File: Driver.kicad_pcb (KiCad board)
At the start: 2 copper layers, 25.5 x 48 mm, 18 parts, among them J1 Screw_Terminal_01x05, U1 IS31FL3239, U2 AP2204K-ADJ

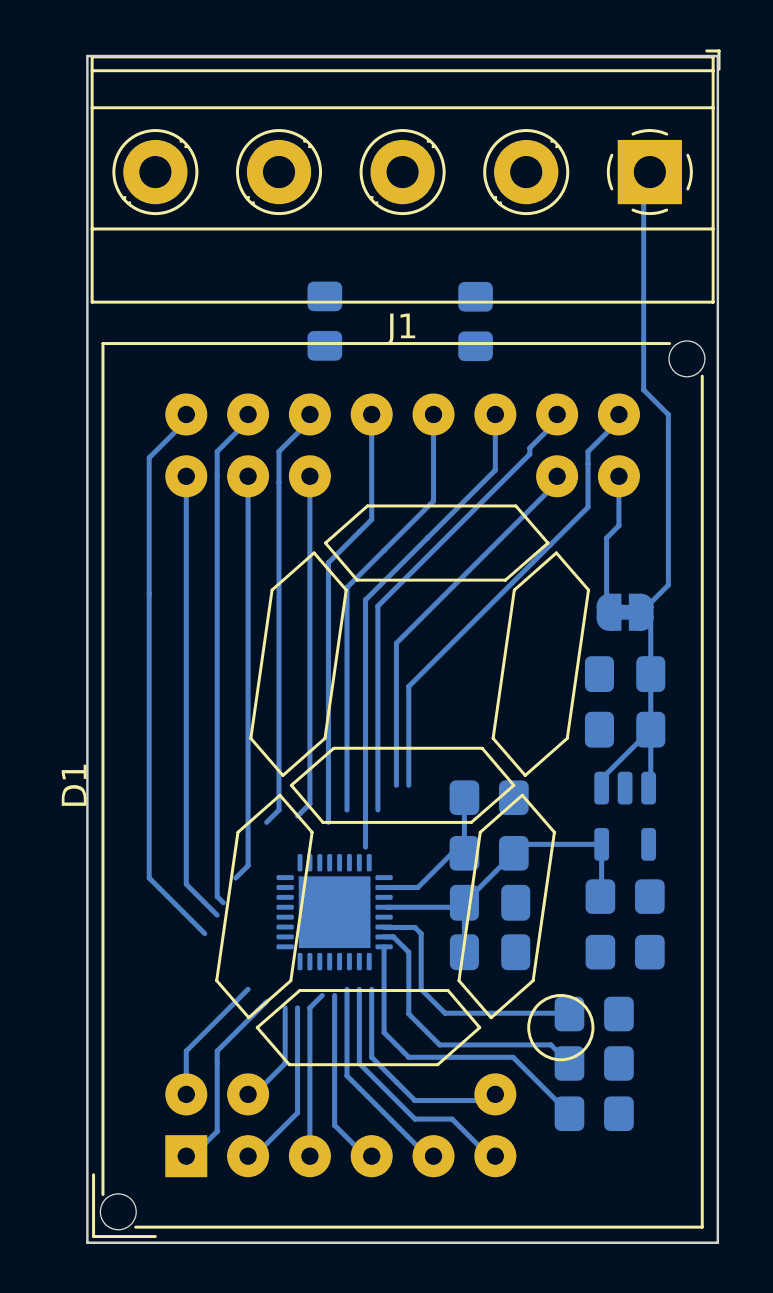
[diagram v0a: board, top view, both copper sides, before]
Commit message: PCB shows no errors, needs improvements before prototype
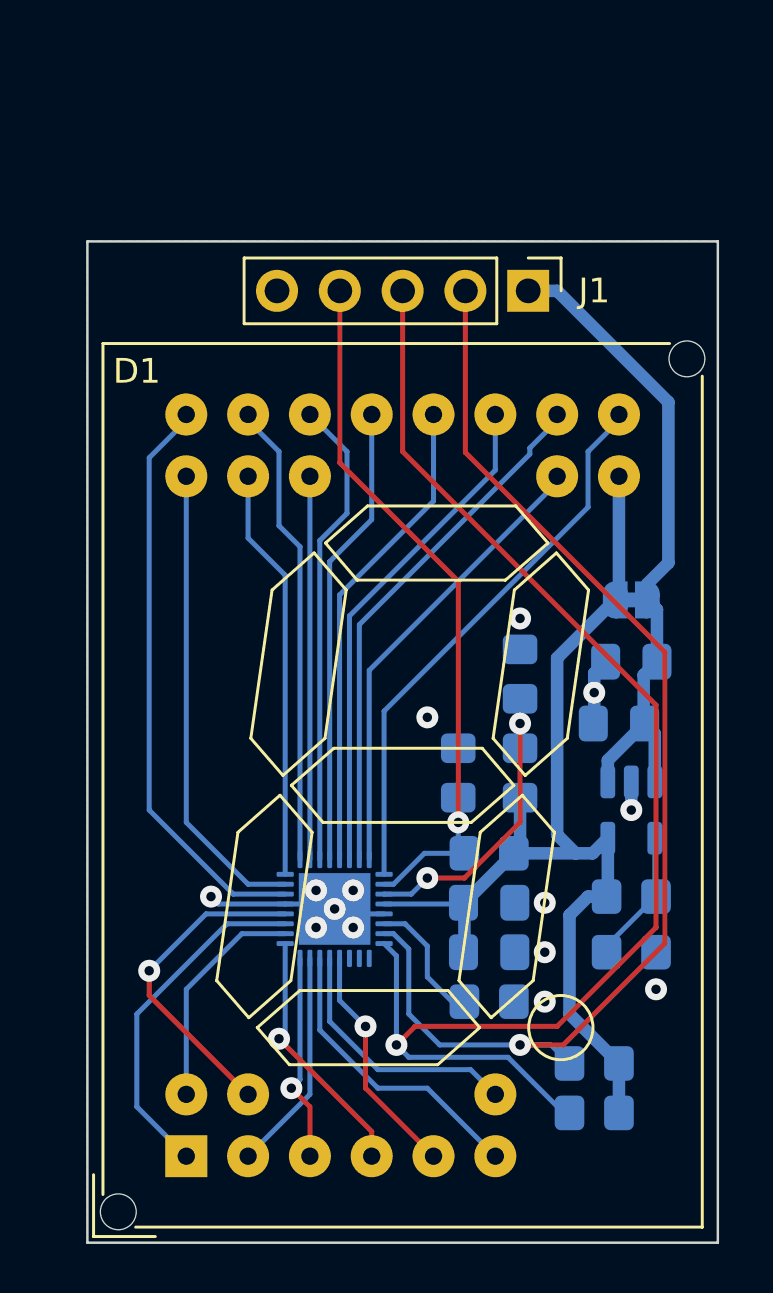
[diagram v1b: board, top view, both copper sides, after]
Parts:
- J1: value Screw_Terminal_01x05 -> Conn_01x05_Socket; footprint TerminalBlock_Phoenix:TerminalBlock_Phoenix_MKDS-1,5-5_1x05_P5.00mm_Horizontal -> Connector_PinHeader_2.54mm:PinHeader_1x05_P2.54mm_Vertical
- moved R4 18.3 mm to (205.0, 99.0)
- moved R10 16.3 mm to (205.0, 95.0)
- moved J1 6.88 mm to (205.3, 79.5), turned to -90 degrees
- moved R11 4.28 mm to (203.8, 108.2)
- moved R3 1.60 mm to (202.5, 99.0), turned to 90 degrees
- moved C2 0.56 mm to (209.5, 94.5)
- moved JP1 0.56 mm to (209.5, 92.0)
- moved C1 0.35 mm to (209.0, 97.0)
- moved U2 0.35 mm to (209.5, 100.5)
- moved R5 0.25 mm to (209.5, 104.0)
- moved R7 0.25 mm to (209.5, 106.2)
- moved U1 0.13 mm to (197.5, 104.5)
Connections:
- U1 pad 1: /LED_R1 -> unconnected-(U1-OUT1-Pad1)
- U1 pad 10: /LED_R4 -> /LED_B5
- U1 pad 11: /LED_G4 -> /LED_G5
- U1 pad 12: /LED_B4 -> /LED_R5
- U1 pad 14: /LED_R5 -> /LED_B6
- U1 pad 15: /LED_G5 -> /LED_G6
- U1 pad 16: /LED_B5 -> /LED_R6
- U1 pad 17: /LED_R6 -> /LED_B7
- U1 pad 18: /LED_G6 -> /LED_G7
- U1 pad 19: /LED_B6 -> /LED_R7
- U1 pad 2: /LED_G1 -> unconnected-(U1-OUT2-Pad2)
- U1 pad 20: /LED_R7 -> /LED_B1
- U1 pad 21: /LED_G7 -> /LED_G1
- U1 pad 22: /LED_B7 -> /LED_R1
- U1 pad 23: unconnected-(U1-OUT22-Pad23) -> /LED_B2
- U1 pad 24: unconnected-(U1-OUT23-Pad24) -> /LED_G2
- U1 pad 25: unconnected-(U1-OUT24-Pad25) -> /LED_R2
- U1 pad 3: /LED_B1 -> unconnected-(U1-OUT3-Pad3)
- U1 pad 4: /LED_R2 -> /LED_B3
- U1 pad 5: /LED_G2 -> /LED_G3
- U1 pad 6: /LED_B2 -> /LED_R3
- U1 pad 7: /LED_R3 -> /LED_B4
- U1 pad 8: /LED_G3 -> /LED_G4
- U1 pad 9: /LED_B3 -> /LED_R4
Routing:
- net /SCL: track 12.3 -> 54.9 mm, vias 0 -> 1
- net /SDA: track 11.1 -> 48.5 mm, vias 0 -> 1
- net VCC: track 19.4 -> 44.0 mm
- net /~{SDB}: track 5.99 -> 29.6 mm, vias 0 -> 1
- net /AD: track 0.00 -> 12.7 mm, vias 0 -> 2
- net GND: track 0.00 -> 11.7 mm, vias 0 -> 14
- net /LED_R5: track 4.37 -> 13.1 mm, vias 0 -> 1
- net /LED_G5: track 7.85 -> 14.1 mm
- net Net-(U2-ADJ): track 0.00 -> 5.46 mm
- net Net-(U1-ISET): track 10.3 -> 5.29 mm
- net /LED_R2: track 18.3 -> 22.3 mm
- net /LED_B5: track 5.54 -> 9.18 mm
- net /LED_G2: track 14.9 -> 18.4 mm
- net /LED_R4: track 7.37 -> 10.3 mm, vias 0 -> 1
- net /V_{in}: track 29.2 -> 26.8 mm
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- added copper zone on B.Cu, net GND
- added copper zone on F.Cu, net GND
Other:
- board size 25.5 x 48 mm -> 25.5 x 40.5 mm

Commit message: More updates/work. Close to finished board
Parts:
- removed C1: 1u, Capacitor_SMD:C_0805_2012Metric_Pad1.18x1.45mm_HandSolder
- removed C2: 0.1u, Capacitor_SMD:C_0805_2012Metric_Pad1.18x1.45mm_HandSolder
- removed JP1: Jumper_2_Bridged, Jumper:SolderJumper-2_P1.3mm_Bridged_RoundedPad1.0x1.5mm
- removed R7: 3.3k, Resistor_SMD:R_0805_2012Metric_Pad1.20x1.40mm_HandSolder
- removed U2: AP2204K-ADJ, Package_TO_SOT_SMD:SOT-23-5
- added J2: Conn_01x05_Socket, ProjectLibrary:CustomBoardInterconnectMirror, B.Cu at (191.5, 106.2)
- added J3: Conn_01x05_Pin, ProjectLibrary:CustomBoardInterconnect, B.Cu at (213.0, 106.2)
- added R6: 0, Resistor_SMD:R_0805_2012Metric_Pad1.20x1.40mm_HandSolder, B.Cu at (207.0, 98.5)
- R5: value 3.3k -> 0
- moved R5 9.82 mm to (207.0, 94.5), turned to -90 degrees
- moved R4 4.53 mm to (204.5, 94.5), turned to -90 degrees
- moved R10 3.54 mm to (204.5, 98.5), turned to 90 degrees
- moved R1 1.46 mm to (208.8, 114.0)
- moved R2 1.25 mm to (208.8, 111.8)
- moved R3 0.50 mm to (202.0, 99.0)
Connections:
- J1 pad 1: /V_{in} -> VCC
- J1 pad 4: /~{SDB} -> GND
- J1 pad 5: GND -> /~{SDB}
- R5 pad 1: VCC -> /SDA
- R5 pad 2: Net-(U2-ADJ) -> /AD
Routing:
- net /~{SDB}: track 29.6 -> 103.2 mm, vias 1 -> 4
- net /SCL: track 54.9 -> 98.0 mm, vias 1 -> 4
- net VCC: track 44.0 -> 85.0 mm, vias 0 -> 2
- net /SDA: track 48.5 -> 87.9 mm, vias 1 -> 4
- net /V_{in}: track 26.8 -> 0.00 mm
- net /AD: track 12.7 -> 18.5 mm
- net Net-(U2-ADJ): track 5.46 -> 0.00 mm
- net GND: track 11.7 -> 8.06 mm, vias 14 -> 18
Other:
- outline, holes or cut-outs redrawn
- board text added: "0x44"
- board text added: "0x45"
- board text added: "0x46"
- board text added: "0x47"
- board text added: "AD121F2 Driver Board"
- board text added: "Designed by Electro707"
- board text added: "I2C Bus Selection"
- board text added: "Rev A"

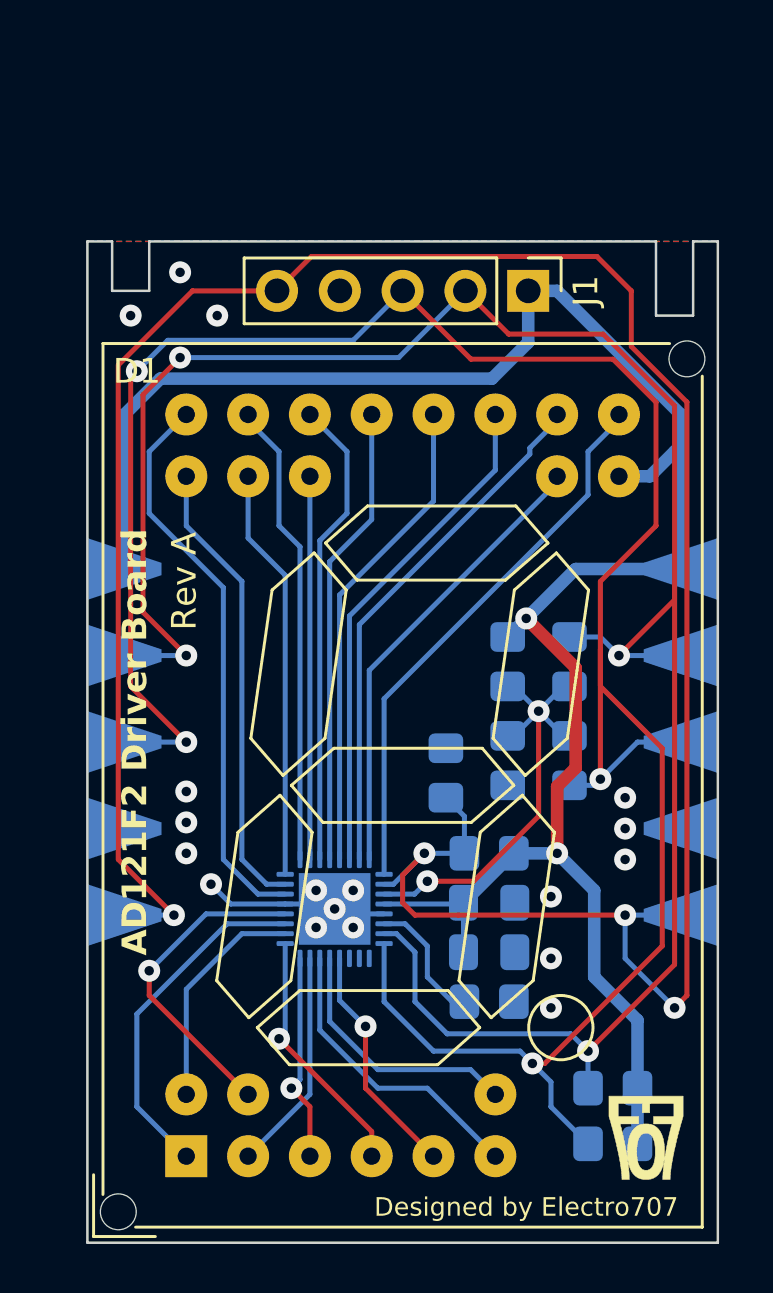
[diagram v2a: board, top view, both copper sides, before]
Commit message: Changed mounting hole placement (gave more clearance between them and side of board)
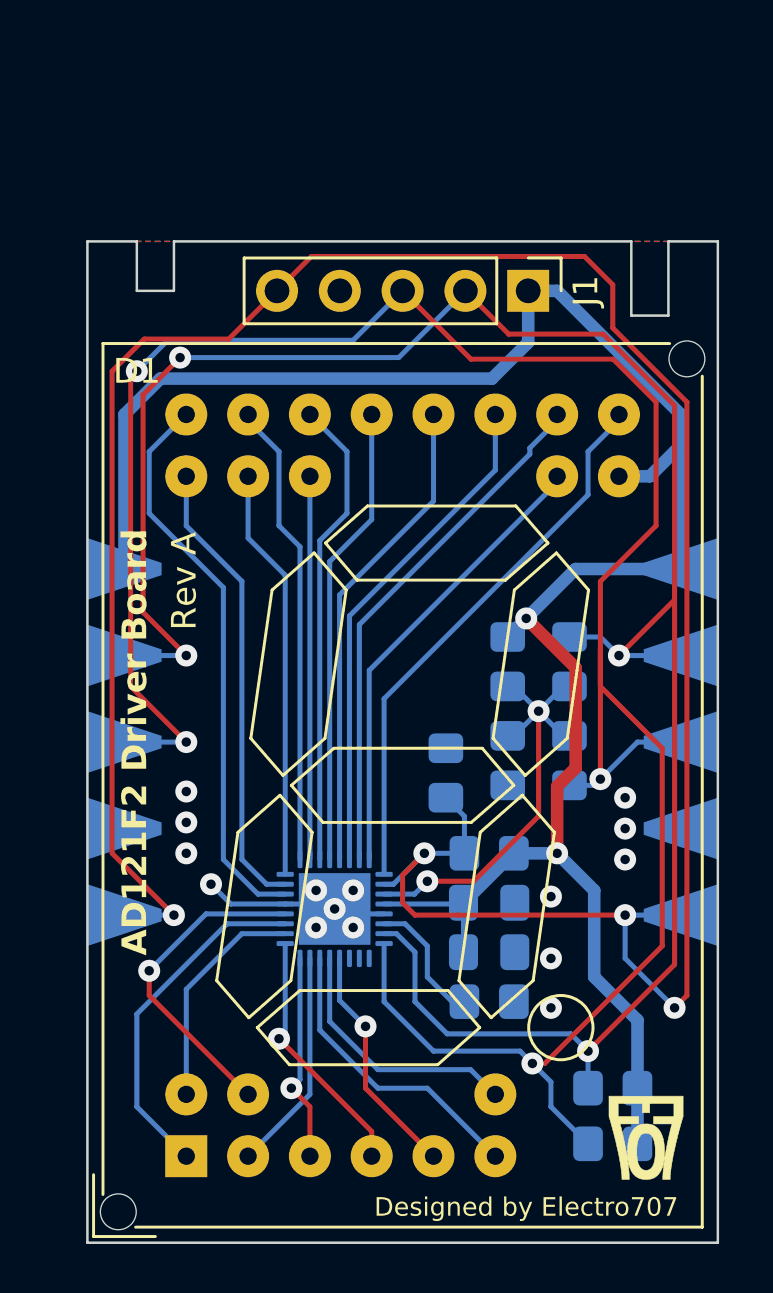
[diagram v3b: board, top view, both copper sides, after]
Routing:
- net GND: vias 18 -> 15
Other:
- outline, holes or cut-outs redrawn
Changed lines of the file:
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@@
     )
     (stroke (width 0.019874) (type solid)) (fill solid) (layer "F.SilkS"))
-  (gr_line (start 210.5 80.5) (end 212 80.5)
-    (stroke (width 0.1) (type default)) (layer "Edge.Cuts"))
-  (gr_line (start 212 77.5) (end 213 77.5)
-    (stroke (width 0.1) (type default)) (layer "Edge.Cuts"))
-  (gr_line (start 190 77.5) (end 210.5 77.5)
+  (gr_line (start 209.5 80.5) (end 211 80.5)
+    (stroke (width 0.1) (type default)) (layer "Edge.Cuts"))
+  (gr_line (start 211 77.5) (end 213 77.5)
+    (stroke (width 0.1) (type default)) (layer "Edge.Cuts"))
+  (gr_line (start 191 77.5) (end 209.5 77.5)
     (stroke (width 0.1) (type default)) (layer "Edge.Cuts"))
   (gr_line (start 187.5 118) (end 187.5 77.5)
     (stroke (width 0.1) (type default)) (layer "Edge.Cuts"))
-  (gr_line (start 212 80.5) (end 212 77.5)
-    (stroke (width 0.1) (type default)) (layer "Edge.Cuts"))
-  (gr_line (start 187.5 77.5) (end 188.5 77.5)
-    (stroke (width 0.1) (type default)) (layer "Edge.Cuts"))
-  (gr_line (start 190 79.5) (end 190 77.5)
-    (stroke (width 0.1) (type default)) (layer "Edge.Cuts"))
-  (gr_line (start 188.5 77.5) (end 188.5 79.5)
+  (gr_line (start 211 80.5) (end 211 77.5)
+    (stroke (width 0.1) (type default)) (layer "Edge.Cuts"))
+  (gr_line (start 187.5 77.5) (end 189.5 77.5)
+    (stroke (width 0.1) (type default)) (layer "Edge.Cuts"))
+  (gr_line (start 191 79.5) (end 191 77.5)
+    (stroke (width 0.1) (type default)) (layer "Edge.Cuts"))
+  (gr_line (start 189.5 77.5) (end 189.5 79.5)
     (stroke (width 0.1) (type default)) (layer "Edge.Cuts"))
   (gr_line (start 213 77.5) (end 213 118)
     (stroke (width 0.1) (type default)) (layer "Edge.Cuts"))
-  (gr_line (start 210.5 77.5) (end 210.5 80.5)
-    (stroke (width 0.1) (type default)) (layer "Edge.Cuts"))
-  (gr_line (start 188.5 79.5) (end 190 79.5)
+  (gr_line (start 209.5 77.5) (end 209.5 80.5)
+    (stroke (width 0.1) (type default)) (layer "Edge.Cuts"))
+  (gr_line (start 189.5 79.5) (end 191 79.5)
     (stroke (width 0.1) (type default)) (layer "Edge.Cuts"))
   (gr_line (start 213 118) (end 187.5 118)
@@
   (via (at 192.5 103.5) (size 0.889) (drill 0.381) (layers "F.Cu" "B.Cu") (net 1))
   (via (at 198.25 105.25) (size 0.889) (drill 0.381) (layers "F.Cu" "B.Cu") (net 1))
-  (via (at 191.25 78.75) (size 0.889) (drill 0.381) (layers "F.Cu" "B.Cu") (net 1))
   (via (at 191.5 101) (size 0.889) (drill 0.381) (layers "F.Cu" "B.Cu") (net 1))
   (via (at 197.5 104.5) (size 0.889) (drill 0.381) (layers "F.Cu" "B.Cu") (net 1))
@@
   (via (at 209.25 101.25) (size 0.889) (drill 0.381) (layers "F.Cu" "B.Cu") (net 1))
   (via (at 191.5 99.75) (size 0.889) (drill 0.381) (layers "F.Cu" "B.Cu") (net 1))
-  (via (at 192.75 80.5) (size 0.889) (drill 0.381) (layers "F.Cu" "B.Cu") (net 1))
   (via (at 209.25 100) (size 0.889) (drill 0.381) (layers "F.Cu" "B.Cu") (net 1))
   (via (at 206.25 108.5) (size 0.889) (drill 0.381) (layers "F.Cu" "B.Cu") (net 1))
   (via (at 196.75 105.25) (size 0.889) (drill 0.381) (layers "F.Cu" "B.Cu") (net 1))
-  (via (at 189.25 80.5) (size 0.889) (drill 0.381) (layers "F.Cu" "B.Cu") (net 1))
   (segment (start 199.5 104.7) (end 197.7 104.7) (width 0.2032) (layer "B.Cu") (net 1))
   (segment (start 197.7 104.7) (end 197.5 104.5) (width 0.2032) (layer "B.Cu") (net 1))
@@
   (segment (start 205.00001 110.25) (end 205.5 110.74999) (width 0.2032) (layer "B.Cu") (net 25))
   (segment (start 199.5 105.9) (end 199.5 108.25) (width 0.2032) (layer "B.Cu") (net 25))
-  (segment (start 188.75 102.5) (end 191 104.75) (width 0.2032) (layer "F.Cu") (net 26))
-  (segment (start 208.1096 78.1096) (end 209.5 79.5) (width 0.2032) (layer "F.Cu") (net 26))
+  (segment (start 189.8015 81.4485) (end 188.5 82.75) (width 0.2032) (layer "F.Cu") (net 26))
+  (segment (start 208.75 81) (end 211.75 84) (width 0.2032) (layer "F.Cu") (net 26))
+  (segment (start 201.129948 102.249973) (end 200.25 103.129921) (width 0.2032) (layer "F.Cu") (net 26))
+  (segment (start 195.17 79.5) (end 196.5604 78.1096) (width 0.2032) (layer "F.Cu") (net 26))
+  (segment (start 202.5 104.75) (end 209.25 104.75) (width 0.2032) (layer "F.Cu") (net 26))
+  (segment (start 207.6096 78.1096) (end 208.75 79.25) (width 0.2032) (layer "F.Cu") (net 26))
+  (segment (start 200.25 103.129921) (end 200.25 104.25) (width 0.2032) (layer "F.Cu") (net 26))
   (segment (start 211.75 84) (end 211.75 108) (width 0.2032) (layer "F.Cu") (net 26))
-  (segment (start 196.5604 78.1096) (end 208.1096 78.1096) (width 0.2032) (layer "F.Cu") (net 26))
-  (segment (start 209.5 79.5) (end 209.5 81.75) (width 0.2032) (layer "F.Cu") (net 26))
-  (segment (start 201.129948 102.249973) (end 200.25 103.129921) (width 0.2032) (layer "F.Cu") (net 26))
-  (segment (start 195.17 79.5) (end 191.75 79.5) (width 0.2032) (layer "F.Cu") (net 26))
-  (segment (start 188.75 82.5) (end 188.75 102.5) (width 0.2032) (layer "F.Cu") (net 26))
-  (segment (start 202.5 104.75) (end 209.25 104.75) (width 0.2032) (layer "F.Cu") (net 26))
-  (segment (start 200.25 103.129921) (end 200.25 104.25) (width 0.2032) (layer "F.Cu") (net 26))
+  (segment (start 195.17 79.5) (end 193.2215 81.4485) (width 0.2032) (layer "F.Cu") (net 26))
+  (segment (start 193.2215 81.4485) (end 189.8015 81.4485) (width 0.2032) (layer "F.Cu") (net 26))
+  (segment (start 200.75 104.75) (end 202.5 104.75) (width 0.2032) (layer "F.Cu") (net 26))
+  (segment (start 196.5604 78.1096) (end 207.6096 78.1096) (width 0.2032) (layer "F.Cu") (net 26))
+  (segment (start 208.75 79.25) (end 208.75 81) (width 0.2032) (layer "F.Cu") (net 26))
+  (segment (start 188.5 82.75) (end 188.5 102.25) (width 0.2032) (layer "F.Cu") (net 26))
+  (segment (start 188.5 102.25) (end 191 104.75) (width 0.2032) (layer "F.Cu") (net 26))
   (segment (start 211.75 108) (end 211.25 108.5) (width 0.2032) (layer "F.Cu") (net 26))
-  (segment (start 200.75 104.75) (end 202.5 104.75) (width 0.2032) (layer "F.Cu") (net 26))
-  (segment (start 195.17 79.5) (end 196.5604 78.1096) (width 0.2032) (layer "F.Cu") (net 26))
-  (segment (start 191.75 79.5) (end 188.75 82.5) (width 0.2032) (layer "F.Cu") (net 26))
-  (segment (start 209.5 81.75) (end 211.75 84) (width 0.2032) (layer "F.Cu") (net 26))
   (segment (start 200.25 104.25) (end 200.75 104.75) (width 0.2032) (layer "F.Cu") (net 26))
   (via (at 211.25 108.5) (size 0.889) (drill 0.381) (layers "F.Cu" "B.Cu") (net 26))
@@
   (group "" (id 2f0d3f0e-0ce2-4d65-9a6a-a2856de60ebf)
     (members
-      15906297-292b-46c4-9451-6bcd500f4ba8
       33b45a6a-f4c8-432a-934e-021d49f335e3
       78d26959-f011-4ebd-9d48-4547cbabbe44

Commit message: Finalization stuff
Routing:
- net GND: track 8.06 -> 13.3 mm
